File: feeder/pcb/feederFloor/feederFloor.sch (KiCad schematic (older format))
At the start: 2 parts, among them J1 Conn_01x08_Female, J2 JST_XH

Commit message: updated schematic to have five connectors
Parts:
- removed J1: Conn_01x08_Female, stephen:70AA, symbol Connector:Conn_01x08_Female
- removed J2: JST_XH, Connector_JST:JST_PH_S4B-PH-SM4-TB_1x04-1MP_P2.00mm_Horizontal, symbol Connector:Conn_01x04_Male
- added J1: JST_XH, Connector_JST:JST_XH_B5B-XH-A_1x05_P2.50mm_Vertical, symbol Connector:Conn_01x05_Male
- added J2: Conn_01x10_Female, symbol Connector:Conn_01x10_Female
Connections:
- wire segments 16 -> 20
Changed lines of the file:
@@
 $EndDescr
 $Comp
-L Connector:Conn_01x04_Male J2
-U 1 1 5E33740D
-P 4000 2950
-F 0 "J2" V 4154 2662 50  0000 R CNN
-F 1 "JST_XH" V 4063 2662 50  0000 R CNN
-F 2 "Connector_JST:JST_PH_S4B-PH-SM4-TB_1x04-1MP_P2.00mm_Horizontal" H 4000 2950 50  0001 C CNN
-F 3 "~" H 4000 2950 50  0001 C CNN
-	1    4000 2950
+L Connector:Conn_01x10_Female J2
+U 1 1 5F87581F
+P 5600 1750
+F 0 "J2" V 5765 1680 50  0000 C CNN
+F 1 "Conn_01x10_Female" V 5674 1680 50  0000 C CNN
+F 2 "" H 5600 1750 50  0001 C CNN
+F 3 "~" H 5600 1750 50  0001 C CNN
+	1    5600 1750
+	0    -1   -1   0
+$EndComp
+$Comp
+L Connector:Conn_01x05_Male J1
+U 1 1 5F877577
+P 5400 2750
+F 0 "J1" V 5554 2462 50  0000 R CNN
+F 1 "JST_XH" V 5463 2462 50  0000 R CNN
+F 2 "Connector_JST:JST_XH_B5B-XH-A_1x05_P2.50mm_Vertical" H 5400 2750 50  0001 C CNN
+F 3 "~" H 5400 2750 50  0001 C CNN
+	1    5400 2750
 	0    -1   -1   0
 $EndComp
 Wire Wire Line
-	4200 2150 4200 2300
+	5200 1950 5200 2450
 Wire Wire Line
-	4000 2150 4000 2500
-$Comp
-L Connector:Conn_01x08_Female J1
-U 1 1 5E33A1A9
-P 4200 1950
-F 0 "J1" V 4365 1880 50  0000 C CNN
-F 1 "Conn_01x08_Female" V 4274 1880 50  0000 C CNN
-F 2 "stephen:70AA" H 4200 1950 50  0001 C CNN
-F 3 "~" H 4200 1950 50  0001 C CNN
-	1    4200 1950
-	0    -1   -1   0
-$EndComp
+	5300 1950 5300 2350
 Wire Wire Line
-	4600 2150 4600 2600
+	5400 1950 5400 2250
 Wire Wire Line
-	4600 2600 3900 2600
-Connection ~ 3900 2600
+	5500 1950 5500 2150
 Wire Wire Line
-	3900 2600 3900 2150
+	5600 1950 5600 2050
 Wire Wire Line
-	4500 2150 4500 2500
+	5600 2050 5700 2050
 Wire Wire Line
-	4500 2500 4000 2500
-Connection ~ 4000 2500
+	5700 2050 5700 1950
+Connection ~ 5600 2050
 Wire Wire Line
-	4400 2150 4400 2400
+	5600 2050 5600 2550
 Wire Wire Line
-	4400 2400 4100 2400
-Connection ~ 4100 2400
+	5500 2150 5800 2150
 Wire Wire Line
-	4100 2400 4100 2150
+	5800 2150 5800 1950
+Connection ~ 5500 2150
 Wire Wire Line
-	4300 2150 4300 2300
+	5500 2150 5500 2550
 Wire Wire Line
-	4300 2300 4200 2300
-Connection ~ 4200 2300
+	5400 2250 5900 2250
 Wire Wire Line
-	4000 2500 4000 2750
+	5900 2250 5900 1950
+Connection ~ 5400 2250
 Wire Wire Line
-	4100 2400 4100 2750
+	5400 2250 5400 2550
 Wire Wire Line
-	3900 2600 3900 2750
+	5300 2350 6000 2350
 Wire Wire Line
-	4200 2300 4200 2750
+	6000 2350 6000 1950
+Connection ~ 5300 2350
+Wire Wire Line
+	5300 2350 5300 2550
+Wire Wire Line
+	5200 2450 6100 2450
+Wire Wire Line
+	6100 2450 6100 1950
+Connection ~ 5200 2450
+Wire Wire Line
+	5200 2450 5200 2550
 $EndSCHEMATC

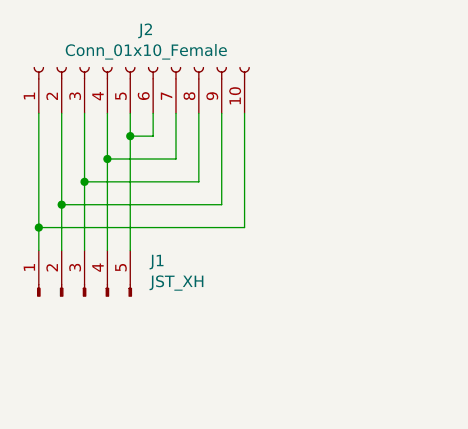
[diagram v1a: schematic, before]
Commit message: added resistors and routed. need to check pinout from rev003 feeder
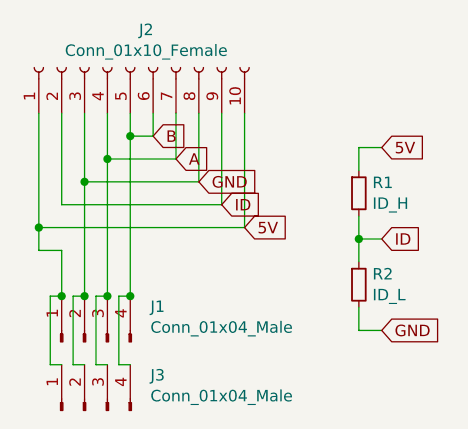
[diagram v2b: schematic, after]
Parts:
- removed J1: JST_XH, Connector_JST:JST_XH_B5B-XH-A_1x05_P2.50mm_Vertical, symbol Connector:Conn_01x05_Male
- added J1, J3: Conn_01x04_Male, Connector_JST:JST_XH_B4B-XH-A_1x04_P2.50mm_Vertical, symbol Connector:Conn_01x04_Male
- added R1: ID_H, Resistor_SMD:R_0805_2012Metric_Pad1.15x1.40mm_HandSolder, symbol Device:R_Small
- added R2: ID_L, Resistor_SMD:R_0805_2012Metric_Pad1.15x1.40mm_HandSolder, symbol Device:R_Small
- J2: footprint (none) -> index:70AA-5
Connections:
- net 5V: now reaches J2.1 (Pin_1), J2.10 (Pin_10)
- net 5V: now also J1.1 (Pin_1), J3.1 (Pin_1), R1.1
- net ID: now reaches J2.2 (Pin_2), J2.9 (Pin_9)
- net ID: now also R1.2, R2.1
- net GND: now reaches J2.3 (Pin_3), J2.8 (Pin_8)
- net GND: now also J1.2 (Pin_2), J3.2 (Pin_2), R2.2
- net A: now reaches J2.4 (Pin_4), J2.7 (Pin_7)
- net A: now also J1.3 (Pin_3), J3.3 (Pin_3)
- net B: now reaches J2.5 (Pin_5), J2.6 (Pin_6)
- net B: now also J1.4 (Pin_4), J3.4 (Pin_4)
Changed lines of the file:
@@
 F 0 "J2" V 5765 1680 50  0000 C CNN
 F 1 "Conn_01x10_Female" V 5674 1680 50  0000 C CNN
-F 2 "" H 5600 1750 50  0001 C CNN
+F 2 "index:70AA-5" H 5600 1750 50  0001 C CNN
 F 3 "~" H 5600 1750 50  0001 C CNN
 	1    5600 1750
-	0    -1   -1   0
-$EndComp
-$Comp
-L Connector:Conn_01x05_Male J1
-U 1 1 5F877577
-P 5400 2750
-F 0 "J1" V 5554 2462 50  0000 R CNN
-F 1 "JST_XH" V 5463 2462 50  0000 R CNN
-F 2 "Connector_JST:JST_XH_B5B-XH-A_1x05_P2.50mm_Vertical" H 5400 2750 50  0001 C CNN
-F 3 "~" H 5400 2750 50  0001 C CNN
-	1    5400 2750
 	0    -1   -1   0
 $EndComp
@@
 Connection ~ 5600 2050
 Wire Wire Line
-	5600 2050 5600 2550
-Wire Wire Line
 	5500 2150 5800 2150
 Wire Wire Line
 	5800 2150 5800 1950
 Connection ~ 5500 2150
-Wire Wire Line
-	5500 2150 5500 2550
 Wire Wire Line
 	5400 2250 5900 2250
@@
 Connection ~ 5400 2250
 Wire Wire Line
-	5400 2250 5400 2550
-Wire Wire Line
 	5300 2350 6000 2350
 Wire Wire Line
 	6000 2350 6000 1950
-Connection ~ 5300 2350
-Wire Wire Line
-	5300 2350 5300 2550
 Wire Wire Line
 	5200 2450 6100 2450
@@
 Wire Wire Line
 	5200 2450 5200 2550
+$Comp
+L Device:R_Small R1
+U 1 1 5F87EC9E
+P 6600 2300
+F 0 "R1" H 6659 2346 50  0000 L CNN
+F 1 "ID_H" H 6659 2255 50  0000 L CNN
+F 2 "Resistor_SMD:R_0805_2012Metric_Pad1.15x1.40mm_HandSolder" H 6600 2300 50  0001 C CNN
+F 3 "~" H 6600 2300 50  0001 C CNN
+	1    6600 2300
+	1    0    0    -1
+$EndComp
+$Comp
+L Device:R_Small R2
+U 1 1 5F87EF44
+P 6600 2700
+F 0 "R2" H 6659 2746 50  0000 L CNN
+F 1 "ID_L" H 6659 2655 50  0000 L CNN
+F 2 "Resistor_SMD:R_0805_2012Metric_Pad1.15x1.40mm_HandSolder" H 6600 2700 50  0001 C CNN
+F 3 "~" H 6600 2700 50  0001 C CNN
+	1    6600 2700
+	1    0    0    -1
+$EndComp
+Text GLabel 6700 2100 2    50   Input ~ 0
+5V
+Text GLabel 6000 2350 2    50   Input ~ 0
+ID
+Text GLabel 5900 2250 2    50   Input ~ 0
+GND
+Text GLabel 5800 2150 2    50   Input ~ 0
+A
+Text GLabel 5700 2050 2    50   Input ~ 0
+B
+Text GLabel 6700 2900 2    50   Input ~ 0
+GND
+Text GLabel 6100 2450 2    50   Input ~ 0
+5V
+Text GLabel 6700 2500 2    50   Input ~ 0
+ID
+Wire Wire Line
+	6700 2100 6600 2100
+Wire Wire Line
+	6600 2100 6600 2200
+Wire Wire Line
+	6600 2400 6600 2500
+Wire Wire Line
+	6600 2800 6600 2900
+Wire Wire Line
+	6600 2900 6700 2900
+Wire Wire Line
+	6700 2500 6600 2500
+Connection ~ 6600 2500
+Wire Wire Line
+	6600 2500 6600 2600
+$Comp
+L Connector:Conn_01x04_Male J1
+U 1 1 5F882F66
+P 5400 2950
+F 0 "J1" V 5554 2662 50  0000 R CNN
+F 1 "Conn_01x04_Male" V 5463 2662 50  0000 R CNN
+F 2 "Connector_JST:JST_XH_B4B-XH-A_1x04_P2.50mm_Vertical" H 5400 2950 50  0001 C CNN
+F 3 "~" H 5400 2950 50  0001 C CNN
+	1    5400 2950
+	0    -1   -1   0
+$EndComp
+Wire Wire Line
+	5200 2550 5300 2550
+Wire Wire Line
+	5300 2550 5300 2750
+Wire Wire Line
+	5400 2250 5400 2750
+Wire Wire Line
+	5500 2150 5500 2750
+Wire Wire Line
+	5600 2050 5600 2750
+$Comp
+L Connector:Conn_01x04_Male J3
+U 1 1 5F885B20
+P 5400 3250
+F 0 "J3" V 5554 2962 50  0000 R CNN
+F 1 "Conn_01x04_Male" V 5463 2962 50  0000 R CNN
+F 2 "Connector_JST:JST_XH_B4B-XH-A_1x04_P2.50mm_Vertical" H 5400 3250 50  0001 C CNN
+F 3 "~" H 5400 3250 50  0001 C CNN
+	1    5400 3250
+	0    -1   -1   0
+$EndComp
+Wire Wire Line
+	5400 2750 5350 2750
+Wire Wire Line
+	5350 2750 5350 3050
+Wire Wire Line
+	5350 3050 5400 3050
+Connection ~ 5400 2750
+Wire Wire Line
+	5500 2750 5450 2750
+Wire Wire Line
+	5450 2750 5450 3050
+Wire Wire Line
+	5450 3050 5500 3050
+Connection ~ 5500 2750
+Wire Wire Line
+	5600 2750 5550 2750
+Wire Wire Line
+	5550 2750 5550 3050
+Wire Wire Line
+	5550 3050 5600 3050
+Connection ~ 5600 2750
+Wire Wire Line
+	5300 2750 5250 2750
+Wire Wire Line
+	5250 2750 5250 3050
+Wire Wire Line
+	5250 3050 5300 3050
+Connection ~ 5300 2750
 $EndSCHEMATC

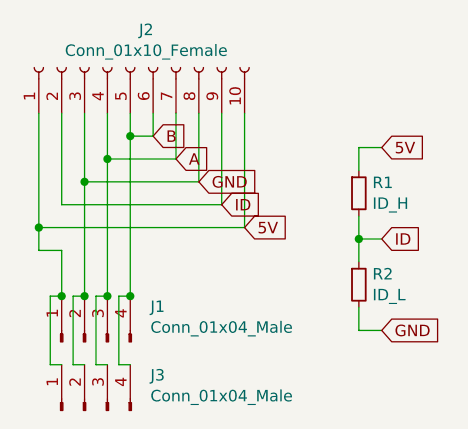
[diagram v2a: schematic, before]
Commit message: fixed routing to match rev003 feeder spring finger pinout
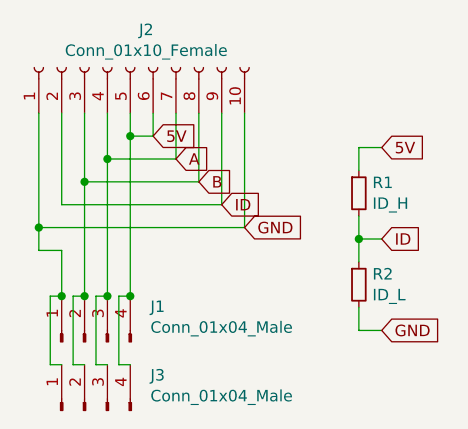
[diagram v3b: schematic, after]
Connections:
- net 5V: now also J1.4 (Pin_4), J2.5 (Pin_5), J2.6 (Pin_6), J3.4 (Pin_4); no longer J1.1 (Pin_1), J2.1 (Pin_1), J2.10 (Pin_10), J3.1 (Pin_1)
- net B: now also J1.2 (Pin_2), J2.3 (Pin_3), J2.8 (Pin_8), J3.2 (Pin_2); no longer J1.4 (Pin_4), J2.5 (Pin_5), J2.6 (Pin_6), J3.4 (Pin_4)
- net GND: now also J1.1 (Pin_1), J2.1 (Pin_1), J2.10 (Pin_10), J3.1 (Pin_1); no longer J1.2 (Pin_2), J2.3 (Pin_3), J2.8 (Pin_8), J3.2 (Pin_2)
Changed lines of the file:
@@
 Text GLabel 6000 2350 2    50   Input ~ 0
 ID
-Text GLabel 5900 2250 2    50   Input ~ 0
+Text GLabel 6100 2450 2    50   Input ~ 0
 GND
 Text GLabel 5800 2150 2    50   Input ~ 0
 A
-Text GLabel 5700 2050 2    50   Input ~ 0
+Text GLabel 5900 2250 2    50   Input ~ 0
 B
 Text GLabel 6700 2900 2    50   Input ~ 0
 GND
-Text GLabel 6100 2450 2    50   Input ~ 0
+Text GLabel 5700 2050 2    50   Input ~ 0
 5V
 Text GLabel 6700 2500 2    50   Input ~ 0

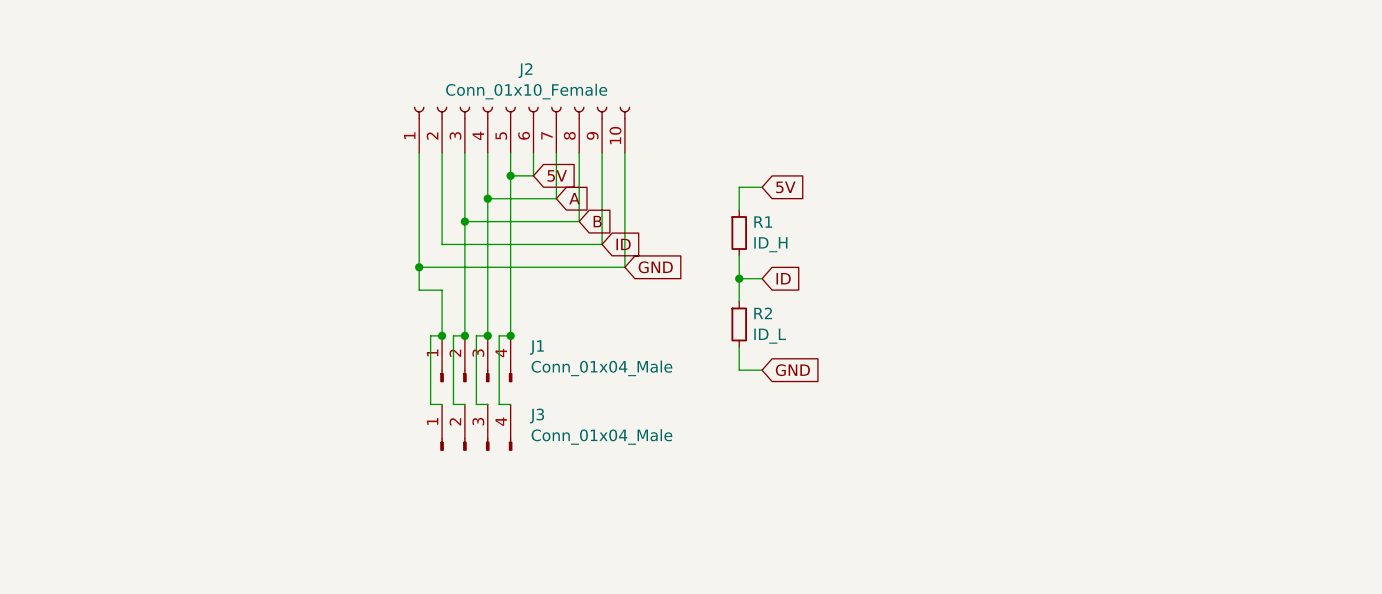
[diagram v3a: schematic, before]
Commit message: this commit reflects boards ordered for rev04 of the feeder motherboard, rev02 of the indexing wheel, and rev02 of the feeder floor
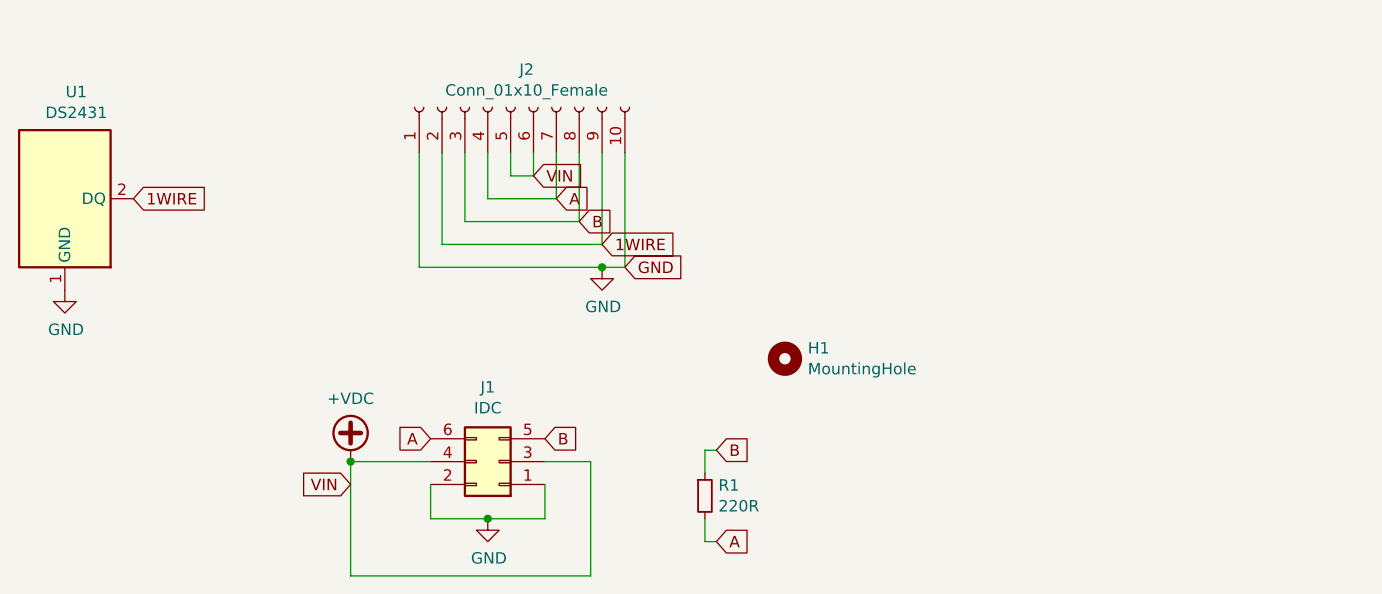
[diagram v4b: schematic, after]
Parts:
- removed J1, J3: Conn_01x04_Male, Connector_JST:JST_XH_B4B-XH-A_1x04_P2.50mm_Vertical, symbol Connector:Conn_01x04_Male
- removed R2: ID_L, Resistor_SMD:R_0805_2012Metric_Pad1.15x1.40mm_HandSolder, symbol Device:R_Small
- added H1: MountingHole, MountingHole:MountingHole_5.3mm_M5, symbol Mechanical:MountingHole
- added J1: IDC, Connector_IDC:IDC-Header_2x03_P2.54mm_Vertical, symbol Connector_Generic:Conn_02x03_Odd_Even
- added U1: DS2431, Package_SO_J-Lead:TSOC-6_3.76x3.94mm_P1.27mm, symbol index:DS2431
- R1: value ID_H -> 220R
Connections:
- net A: now also R1.2, J1.6 (Pin_6)
- net B: now also R1.1, J1.5 (Pin_5)
- net GND: now also J1.1 (Pin_1), J1.2 (Pin_2), U1.1 (GND)
- net 5V renamed +VDC
- net +VDC: now also J1.3 (Pin_3), J1.4 (Pin_4); no longer R1.1
- net ID renamed 1WIRE
- net 1WIRE: now also U1.2 (DQ); no longer R1.2
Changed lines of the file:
@@
 Wire Wire Line
 	5700 2050 5700 1950
-Connection ~ 5600 2050
 Wire Wire Line
 	5500 2150 5800 2150
 Wire Wire Line
 	5800 2150 5800 1950
-Connection ~ 5500 2150
 Wire Wire Line
 	5400 2250 5900 2250
 Wire Wire Line
 	5900 2250 5900 1950
-Connection ~ 5400 2250
 Wire Wire Line
 	5300 2350 6000 2350
@@
 	6000 2350 6000 1950
 Wire Wire Line
-	5200 2450 6100 2450
+	5200 2450 6000 2450
 Wire Wire Line
 	6100 2450 6100 1950
-Connection ~ 5200 2450
-Wire Wire Line
-	5200 2450 5200 2550
-$Comp
-L Device:R_Small R1
-U 1 1 5F87EC9E
-P 6600 2300
-F 0 "R1" H 6659 2346 50  0000 L CNN
-F 1 "ID_H" H 6659 2255 50  0000 L CNN
-F 2 "Resistor_SMD:R_0805_2012Metric_Pad1.15x1.40mm_HandSolder" H 6600 2300 50  0001 C CNN
-F 3 "~" H 6600 2300 50  0001 C CNN
-	1    6600 2300
-	1    0    0    -1
-$EndComp
-$Comp
-L Device:R_Small R2
-U 1 1 5F87EF44
-P 6600 2700
-F 0 "R2" H 6659 2746 50  0000 L CNN
-F 1 "ID_L" H 6659 2655 50  0000 L CNN
-F 2 "Resistor_SMD:R_0805_2012Metric_Pad1.15x1.40mm_HandSolder" H 6600 2700 50  0001 C CNN
-F 3 "~" H 6600 2700 50  0001 C CNN
-	1    6600 2700
-	1    0    0    -1
-$EndComp
-Text GLabel 6700 2100 2    50   Input ~ 0
-5V
-Text GLabel 6000 2350 2    50   Input ~ 0
-ID
 Text GLabel 6100 2450 2    50   Input ~ 0
 GND
@@
 Text GLabel 5900 2250 2    50   Input ~ 0
 B
-Text GLabel 6700 2900 2    50   Input ~ 0
-GND
 Text GLabel 5700 2050 2    50   Input ~ 0
-5V
-Text GLabel 6700 2500 2    50   Input ~ 0
-ID
+VIN
+Text GLabel 3950 2150 2    50   Input ~ 0
+1WIRE
+$Comp
+L index:DS2431 U1
+U 1 1 6014B35D
+P 3650 2150
+F 0 "U1" H 3700 2617 50  0000 C CNN
+F 1 "DS2431" H 3700 2526 50  0000 C CNN
+F 2 "Package_SO_J-Lead:TSOC-6_3.76x3.94mm_P1.27mm" H 4700 1800 50  0001 C CNN
+F 3 "http://pdfserv.maximintegrated.com/en/ds/DS2401.pdf" H 3500 2400 50  0001 C CNN
+	1    3650 2150
+	1    0    0    -1
+$EndComp
+$Comp
+L power:GND #PWR0101
+U 1 1 60150D88
+P 3650 2550
+F 0 "#PWR0101" H 3650 2300 50  0001 C CNN
+F 1 "GND" H 3655 2377 50  0000 C CNN
+F 2 "" H 3650 2550 50  0001 C CNN
+F 3 "" H 3650 2550 50  0001 C CNN
+	1    3650 2550
+	1    0    0    -1
+$EndComp
+$Comp
+L power:GND #PWR0102
+U 1 1 601510A5
+P 6000 2450
+F 0 "#PWR0102" H 6000 2200 50  0001 C CNN
+F 1 "GND" H 6005 2277 50  0000 C CNN
+F 2 "" H 6000 2450 50  0001 C CNN
+F 3 "" H 6000 2450 50  0001 C CNN
+	1    6000 2450
+	1    0    0    -1
+$EndComp
+Connection ~ 6000 2450
 Wire Wire Line
-	6700 2100 6600 2100
-Wire Wire Line
-	6600 2100 6600 2200
-Wire Wire Line
-	6600 2400 6600 2500
-Wire Wire Line
-	6600 2800 6600 2900
-Wire Wire Line
-	6600 2900 6700 2900
-Wire Wire Line
-	6700 2500 6600 2500
-Connection ~ 6600 2500
-Wire Wire Line
-	6600 2500 6600 2600
+	6000 2450 6100 2450
 $Comp
-L Connector:Conn_01x04_Male J1
-U 1 1 5F882F66
-P 5400 2950
-F 0 "J1" V 5554 2662 50  0000 R CNN
-F 1 "Conn_01x04_Male" V 5463 2662 50  0000 R CNN
-F 2 "Connector_JST:JST_XH_B4B-XH-A_1x04_P2.50mm_Vertical" H 5400 2950 50  0001 C CNN
-F 3 "~" H 5400 2950 50  0001 C CNN
-	1    5400 2950
-	0    -1   -1   0
+L power:GND #PWR0103
+U 1 1 60159395
+P 5500 3550
+F 0 "#PWR0103" H 5500 3300 50  0001 C CNN
+F 1 "GND" H 5505 3377 50  0000 C CNN
+F 2 "" H 5500 3550 50  0001 C CNN
+F 3 "" H 5500 3550 50  0001 C CNN
+	1    5500 3550
+	1    0    0    -1
 $EndComp
 Wire Wire Line
-	5200 2550 5300 2550
+	5250 3400 5250 3550
 Wire Wire Line
-	5300 2550 5300 2750
+	5250 3550 5500 3550
 Wire Wire Line
-	5400 2250 5400 2750
+	5750 3400 5750 3550
 Wire Wire Line
-	5500 2150 5500 2750
-Wire Wire Line
-	5600 2050 5600 2750
+	5750 3550 5500 3550
+Connection ~ 5500 3550
 $Comp
-L Connector:Conn_01x04_Male J3
-U 1 1 5F885B20
-P 5400 3250
-F 0 "J3" V 5554 2962 50  0000 R CNN
-F 1 "Conn_01x04_Male" V 5463 2962 50  0000 R CNN
-F 2 "Connector_JST:JST_XH_B4B-XH-A_1x04_P2.50mm_Vertical" H 5400 3250 50  0001 C CNN
-F 3 "~" H 5400 3250 50  0001 C CNN
-	1    5400 3250
-	0    -1   -1   0
+L power:+VDC #PWR0104
+U 1 1 6015A417
+P 4900 3300
+F 0 "#PWR0104" H 4900 3200 50  0001 C CNN
+F 1 "+VDC" H 4900 3575 50  0000 C CNN
+F 2 "" H 4900 3300 50  0001 C CNN
+F 3 "" H 4900 3300 50  0001 C CNN
+	1    4900 3300
+	1    0    0    -1
 $EndComp
 Wire Wire Line
-	5400 2750 5350 2750
+	4900 3300 5250 3300
 Wire Wire Line
-	5350 2750 5350 3050
+	4900 3800 5950 3800
 Wire Wire Line
-	5350 3050 5400 3050
-Connection ~ 5400 2750
+	5950 3800 5950 3300
 Wire Wire Line
-	5500 2750 5450 2750
+	5950 3300 5750 3300
 Wire Wire Line
-	5450 2750 5450 3050
+	4900 3300 4900 3800
+Connection ~ 4900 3300
+Text GLabel 5250 3200 0    50   Input ~ 0
+A
+Text GLabel 5750 3200 2    50   Input ~ 0
+B
+Text GLabel 6000 2350 2    50   Input ~ 0
+1WIRE
+Text GLabel 4900 3400 0    50   Input ~ 0
+VIN
+$Comp
+L Connector_Generic:Conn_02x03_Odd_Even J1
+U 1 1 60161293
+P 5550 3300
+F 0 "J1" H 5600 2975 50  0000 C CNN
+F 1 "IDC" H 5600 3066 50  0000 C CNN
+F 2 "Connector_IDC:IDC-Header_2x03_P2.54mm_Vertical" H 5550 3300 50  0001 C CNN
+F 3 "~" H 5550 3300 50  0001 C CNN
+	1    5550 3300
+	-1   0    0    1
+$EndComp
+$Comp
+L Mechanical:MountingHole H1
+U 1 1 60165998
+P 6800 2850
+F 0 "H1" H 6900 2896 50  0000 L CNN
+F 1 "MountingHole" H 6900 2805 50  0000 L CNN
+F 2 "MountingHole:MountingHole_5.3mm_M5" H 6800 2850 50  0001 C CNN
+F 3 "~" H 6800 2850 50  0001 C CNN
+	1    6800 2850
+	1    0    0    -1
+$EndComp
+$Comp
+L Device:R_Small R1
+U 1 1 6016BC1C
+P 6450 3450
+F 0 "R1" H 6509 3496 50  0000 L CNN
+F 1 "220R" H 6509 3405 50  0000 L CNN
+F 2 "Resistor_SMD:R_0805_2012Metric_Pad1.15x1.40mm_HandSolder" H 6450 3450 50  0001 C CNN
+F 3 "~" H 6450 3450 50  0001 C CNN
+	1    6450 3450
+	1    0    0    -1
+$EndComp
+Text GLabel 6500 3250 2    50   Input ~ 0
+B
+Text GLabel 6500 3650 2    50   Input ~ 0
+A
 Wire Wire Line
-	5450 3050 5500 3050
-Connection ~ 5500 2750
+	6500 3250 6450 3250
 Wire Wire Line
-	5600 2750 5550 2750
+	6450 3250 6450 3350
 Wire Wire Line
-	5550 2750 5550 3050
+	6450 3550 6450 3650
 Wire Wire Line
-	5550 3050 5600 3050
-Connection ~ 5600 2750
-Wire Wire Line
-	5300 2750 5250 2750
-Wire Wire Line
-	5250 2750 5250 3050
-Wire Wire Line
-	5250 3050 5300 3050
-Connection ~ 5300 2750
+	6450 3650 6500 3650
 $EndSCHEMATC

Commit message: Updates to build the appropriate JLCPCB outputs.
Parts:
- R1: JLCPCB (none) -> C17557
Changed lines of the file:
@@
 F 2 "Resistor_SMD:R_0805_2012Metric_Pad1.15x1.40mm_HandSolder" H 6450 3450 50  0001 C CNN
 F 3 "~" H 6450 3450 50  0001 C CNN
+F 4 "C17557" H 6450 3450 50  0001 C CNN "JLCPCB"
 	1    6450 3450
 	1    0    0    -1

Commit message: Updating the package of the resistor on the feeder floor.
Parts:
- R1: footprint Resistor_SMD:R_0805_2012Metric_Pad1.15x1.40mm_HandSolder -> Resistor_SMD:R_0805_2012Metric
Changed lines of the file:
@@
 F 0 "R1" H 6509 3496 50  0000 L CNN
 F 1 "220R" H 6509 3405 50  0000 L CNN
-F 2 "Resistor_SMD:R_0805_2012Metric_Pad1.15x1.40mm_HandSolder" H 6450 3450 50  0001 C CNN
+F 2 "Resistor_SMD:R_0805_2012Metric" H 6450 3450 50  0001 C CNN
 F 3 "~" H 6450 3450 50  0001 C CNN
 F 4 "C17557" H 6450 3450 50  0001 C CNN "JLCPCB"
